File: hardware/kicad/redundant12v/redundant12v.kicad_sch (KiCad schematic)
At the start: 10 parts, among them U1 ATtiny212-SS, U2 MAX232CPE, X1 CXO_DIP8

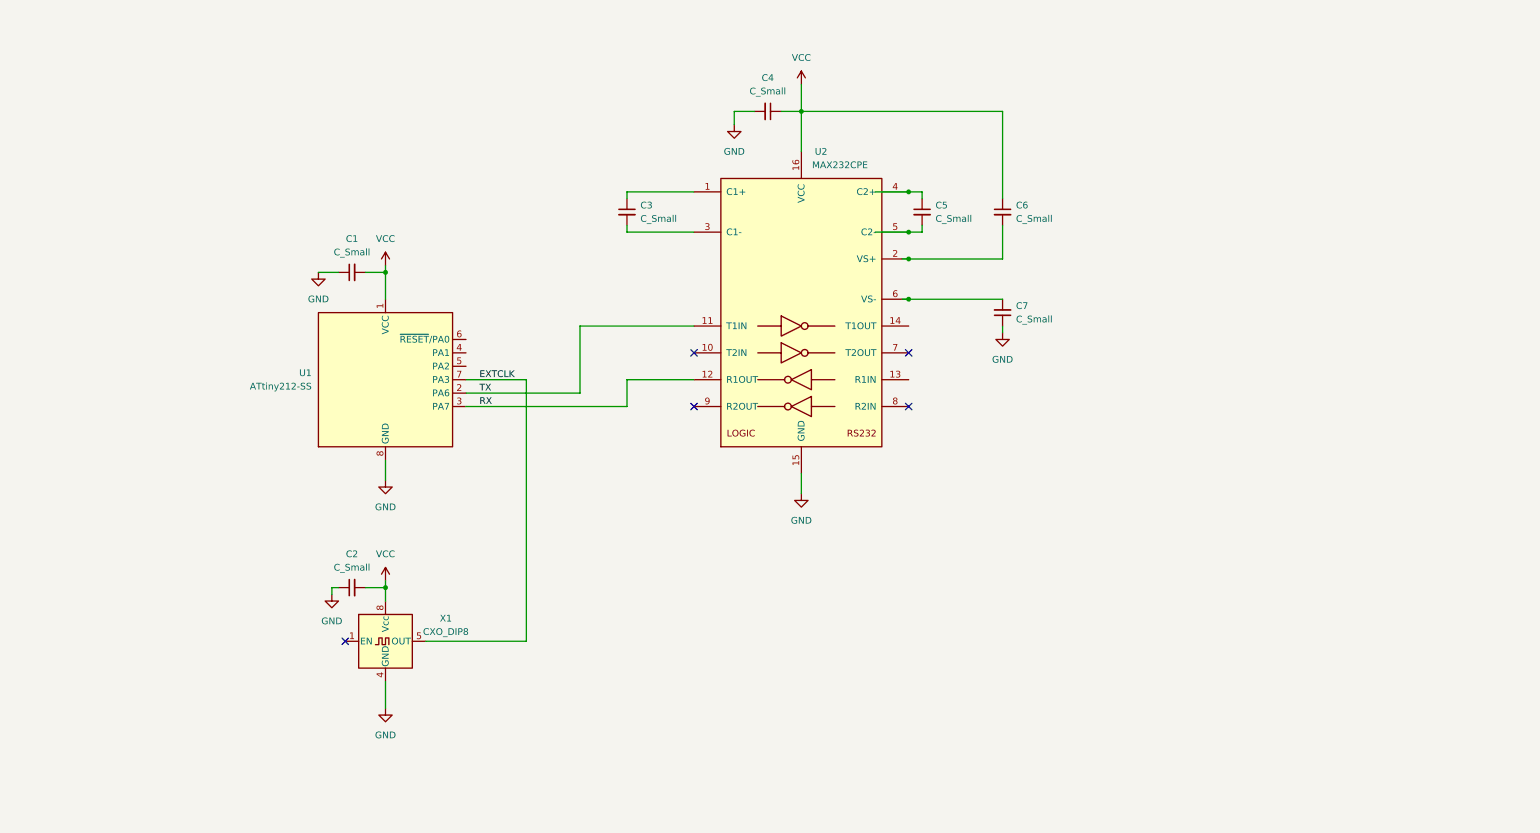
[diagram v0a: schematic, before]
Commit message: Add regulator circuit and LED drivers
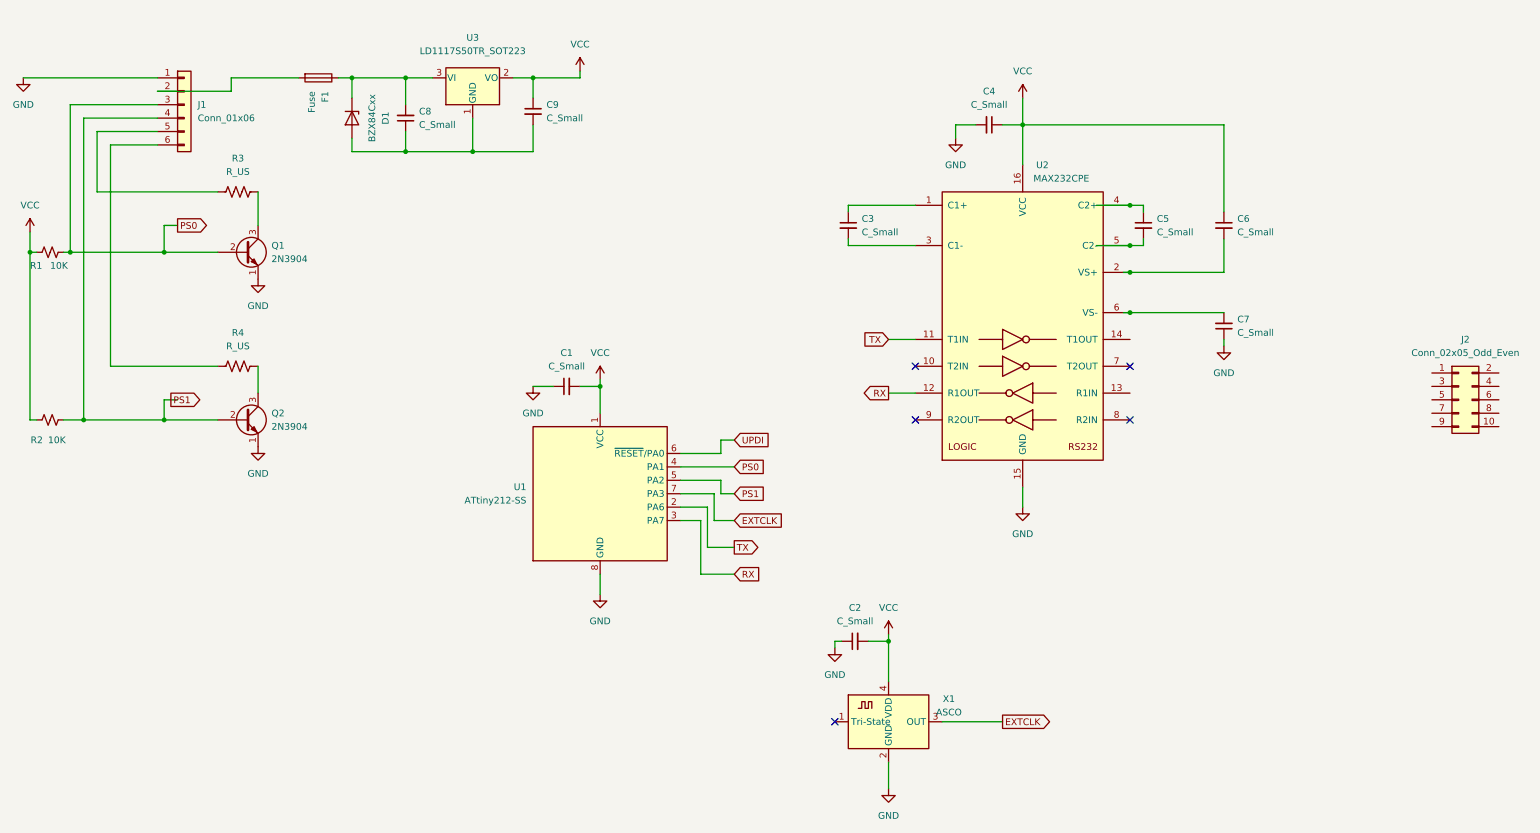
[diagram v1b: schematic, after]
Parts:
- removed X1: CXO_DIP8, Oscillator:Oscillator_DIP-8, symbol Oscillator:CXO_DIP8
- added C8, C9: C_Small, Capacitor_SMD:C_0805_2012Metric_Pad1.18x1.45mm_HandSolder, symbol Device:C_Small
- added D1: BZX84Cxx, Package_TO_SOT_SMD:SOT-23, symbol Diode:BZX84Cxx
- added F1: Fuse, Fuse:Fuse_1206_3216Metric_Pad1.42x1.75mm_HandSolder, symbol Device:Fuse
- added J1: Conn_01x06, Connector_JST:JST_EH_B6B-EH-A_1x06_P2.50mm_Vertical, symbol Connector_Generic:Conn_01x06
- added J2: Conn_02x05_Odd_Even, Connector_IDC:IDC-Header_2x05_P2.54mm_Vertical, symbol Connector_Generic:Conn_02x05_Odd_Even
- added Q1, Q2: 2N3904, Package_TO_SOT_SMD:SOT-23, symbol Transistor_BJT:2N3904
- added R1, R2: 10K, Resistor_SMD:R_0805_2012Metric_Pad1.20x1.40mm_HandSolder, symbol Device:R_Small_US
- added R3, R4: R_US, Resistor_SMD:R_0805_2012Metric_Pad1.20x1.40mm_HandSolder, symbol Device:R_US
- added U3: LD1117S50TR_SOT223, Package_TO_SOT_SMD:SOT-223-3_TabPin2, symbol Regulator_Linear:LD1117S50TR_SOT223
- added X1: ASCO, Oscillator:Oscillator_SMD_Abracon_ASV-4Pin_7.0x5.1mm_HandSoldering, symbol Oscillator:ASCO
- C1, C2, C3, C4, C5, C6, C7: footprint (none) -> Capacitor_SMD:C_0805_2012Metric_Pad1.18x1.45mm_HandSolder
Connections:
- net EXTCLK: now also X1.3 (OUT)
- net GND: now also J1.1 (Pin_1), Q1.1 (E), Q2.1 (E), X1.2 (GND)
- net VCC: now also C9.1, R1.2, R2.2, U3.2 (VO), X1.4 (VDD)
- net PS0: now reaches U1.4 (PA1)
- net PS0: now also J1.3 (Pin_3), Q1.2 (B), R1.1
- net PS1: now reaches U1.5 (PA2)
- net PS1: now also J1.4 (Pin_4), Q2.2 (B), R2.1
- net UPDI: now reaches U1.6 (~{RESET}/PA0)
- new net: J1.6 (Pin_6), R4.1
- new net: Q2.3 (C), R4.2
- new net: C8.2, D1.3 (K), F1.1, U3.3 (VI)
- new net: F1.2, J1.2 (Pin_2)
- new net: C8.1, C9.2, D1.1 (A), U3.1 (GND)
- new net: J1.5 (Pin_5), R3.1
- new net: Q1.3 (C), R3.2
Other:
- moved on the sheet: C1, C2, C3, C4, C5, C6, C7, U1, U2

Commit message: Reorganize schematic, fix LED polarity
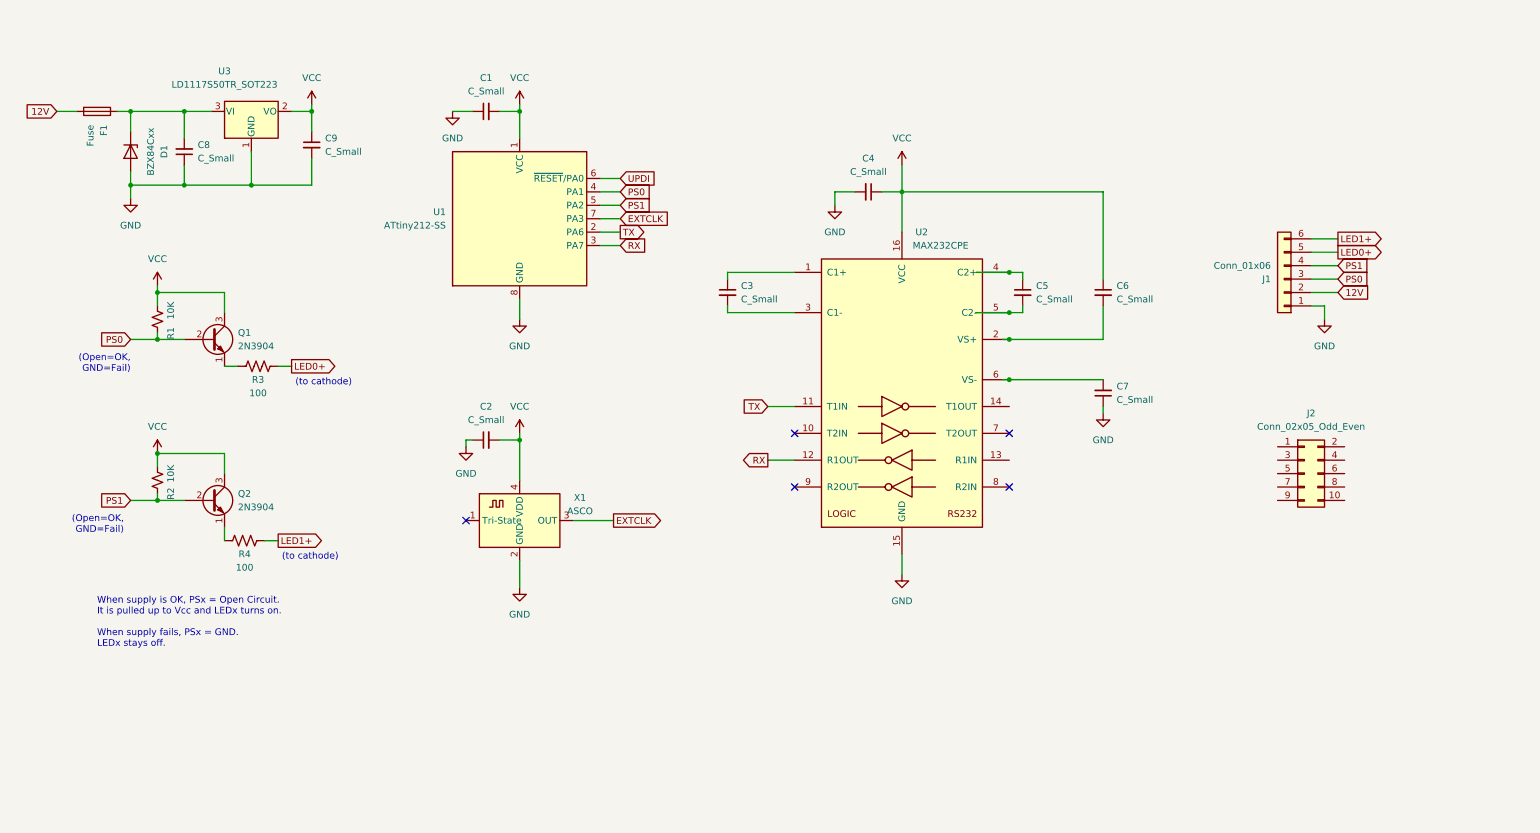
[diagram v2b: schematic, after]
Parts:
- R3, R4: value R_US -> 100
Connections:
- net GND: now also C8.1, C9.2, D1.1 (A), U3.1 (GND); no longer Q1.1 (E), Q2.1 (E)
- net PS0: now also R1.2; no longer R1.1
- net PS1: now also R2.2; no longer R2.1
- net VCC: now also Q1.3 (C), Q2.3 (C), R1.1, R2.1; no longer R1.2, R2.2
- net at R4.1: now also Q2.1 (E); no longer J1.6 (Pin_6)
- net LED1+: now reaches R4.2
- net LED1+: now also J1.6 (Pin_6); no longer Q2.3 (C)
- net 12V: now reaches F1.2, J1.2 (Pin_2)
- net at R3.1: now also Q1.1 (E); no longer J1.5 (Pin_5)
- net LED0+: now reaches R3.2
- net LED0+: now also J1.5 (Pin_5); no longer Q1.3 (C)
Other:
- note added: "(Open=OK, GND=Fail)"
- note added: "(to cathode)"
- note added: "When supply is OK, PSx = Open Circuit. It is pulled up to Vcc and LEDx turns on. When supply fails, PSx = GND. LEDx stays off."
- moved on the sheet: C1, C2, C3, C4, C5, C6, C7, C8, C9, D1, F1, J1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

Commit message: Add serial port connections
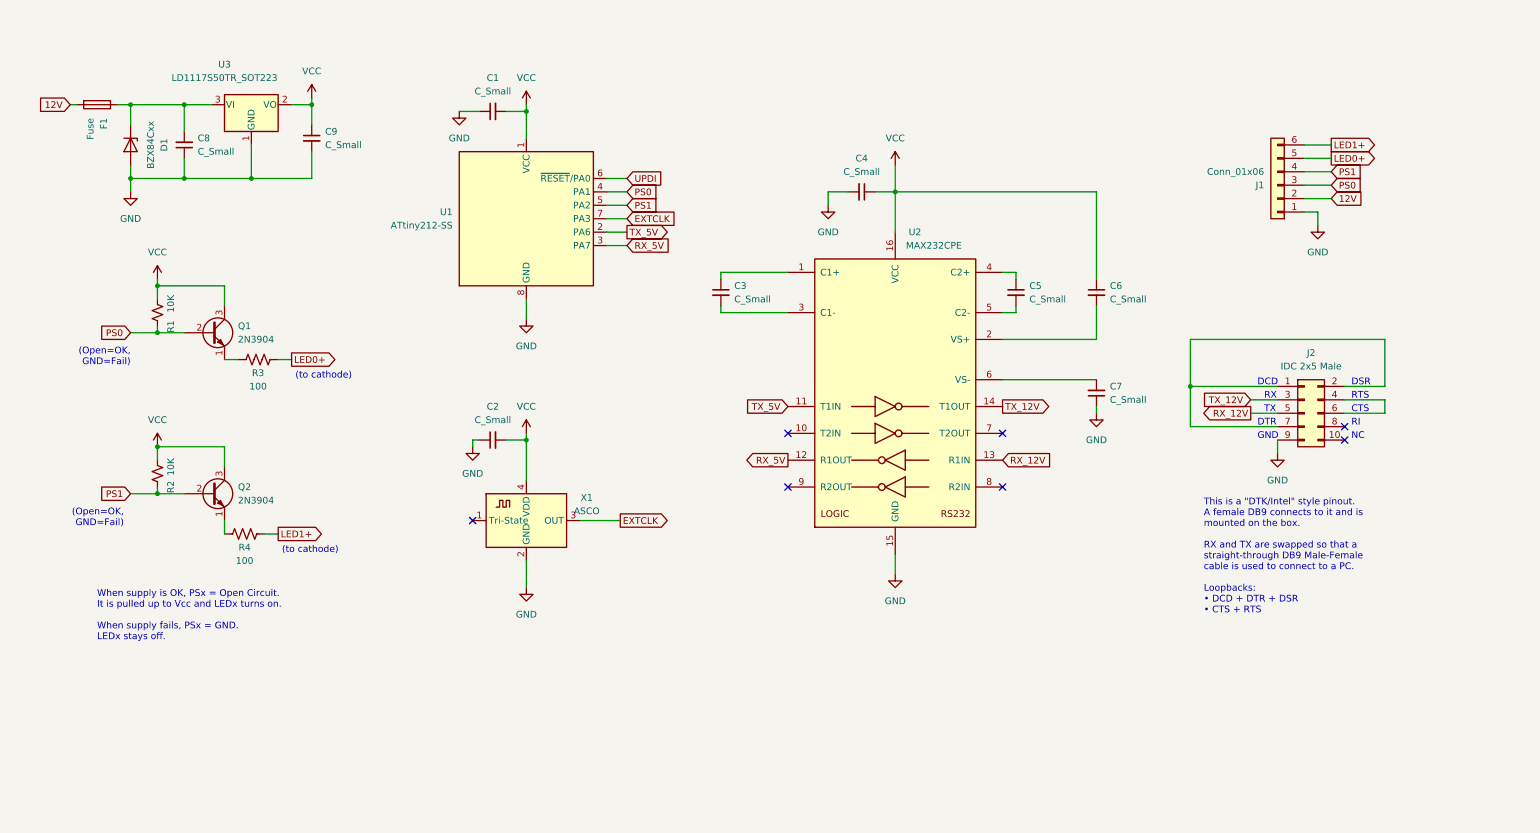
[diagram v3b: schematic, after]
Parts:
- J2: value Conn_02x05_Odd_Even -> IDC 2x5 Male
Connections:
- net GND: now also J2.9 (Pin_9)
- net RX_12V: now reaches U2.13 (R1IN)
- net RX_12V: now also J2.5 (Pin_5)
- net TX_12V: now reaches U2.14 (T1OUT)
- net TX_12V: now also J2.3 (Pin_3)
- net at J2.1 (Pin_1): now also J2.2 (Pin_2), J2.7 (Pin_7)
- net at J2.4 (Pin_4): now also J2.6 (Pin_6)
- net RX renamed RX_5V
- net TX renamed TX_5V
- no-connect marks 5 -> 7
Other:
- note added: "CTS"
- note added: "DCD"
- note added: "DSR"
- note added: "DTR"
- note added: "GND"
- note added: "NC"
- note added: "RI"
- note added: "RTS"
- note added: "RX"
- note added: "TX"
- note added: "This is a "DTK/Intel" style pinout. A female DB9 connects to it and is mounted on the box. RX and TX are swapped so that a straight-through DB9 Male-Female cable is used to connect to a PC. Loopbacks: • DCD + DTR + DSR • CTS + RTS"
- moved on the sheet: C1, C2, C3, C4, C5, C6, C7, C8, C9, D1, F1, J1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

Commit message: PCB is mostly routed
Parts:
- R3, R4: value 100 -> 150
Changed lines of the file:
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@@
     (in_bom yes) (on_board yes)
     (property "Reference" "R4" (id 0) (at 60.96 128.27 90))
-    (property "Value" "100" (id 1) (at 60.96 130.81 90))
+    (property "Value" "150" (id 1) (at 60.96 130.81 90))
     (property "Footprint" "Resistor_SMD:R_0805_2012Metric_Pad1.20x1.40mm_HandSolder" (id 2) (at 61.214 124.714 90)
       (effects (font (size 1.27 1.27)) hide)
@@
     (in_bom yes) (on_board yes)
     (property "Reference" "R3" (id 0) (at 63.5 95.25 90))
-    (property "Value" "100" (id 1) (at 63.5 97.79 90))
+    (property "Value" "150" (id 1) (at 63.5 97.79 90))
     (property "Footprint" "Resistor_SMD:R_0805_2012Metric_Pad1.20x1.40mm_HandSolder" (id 2) (at 63.754 91.694 90)
       (effects (font (size 1.27 1.27)) hide)
@@
     )
     (path "/de0a58e5-7f3d-4ccf-ac8a-4cd50321ae36"
-      (reference "R3") (unit 1) (value "100") (footprint "Resistor_SMD:R_0805_2012Metric_Pad1.20x1.40mm_HandSolder")
+      (reference "R3") (unit 1) (value "150") (footprint "Resistor_SMD:R_0805_2012Metric_Pad1.20x1.40mm_HandSolder")
     )
     (path "/536d55a4-3759-4f62-a47d-eabc58b4f4c3"
-      (reference "R4") (unit 1) (value "100") (footprint "Resistor_SMD:R_0805_2012Metric_Pad1.20x1.40mm_HandSolder")
+      (reference "R4") (unit 1) (value "150") (footprint "Resistor_SMD:R_0805_2012Metric_Pad1.20x1.40mm_HandSolder")
     )
     (path "/18e8ff8f-d1a5-4881-b417-bc839120dcd6"

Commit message: PCB rev 1 finished
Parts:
- added TP1: VTG_5V, TestPoint:TestPoint_Pad_D2.5mm, symbol Connector:TestPoint
- added TP2: UPDI, TestPoint:TestPoint_Pad_D2.5mm, symbol Connector:TestPoint
- added TP3: GND, TestPoint:TestPoint_Pad_D2.5mm, symbol Connector:TestPoint
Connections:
- net GND: now also TP3.1
- net UPDI: now also TP2.1
- net VCC: now also TP1.1
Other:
- moved on the sheet: J1, J2

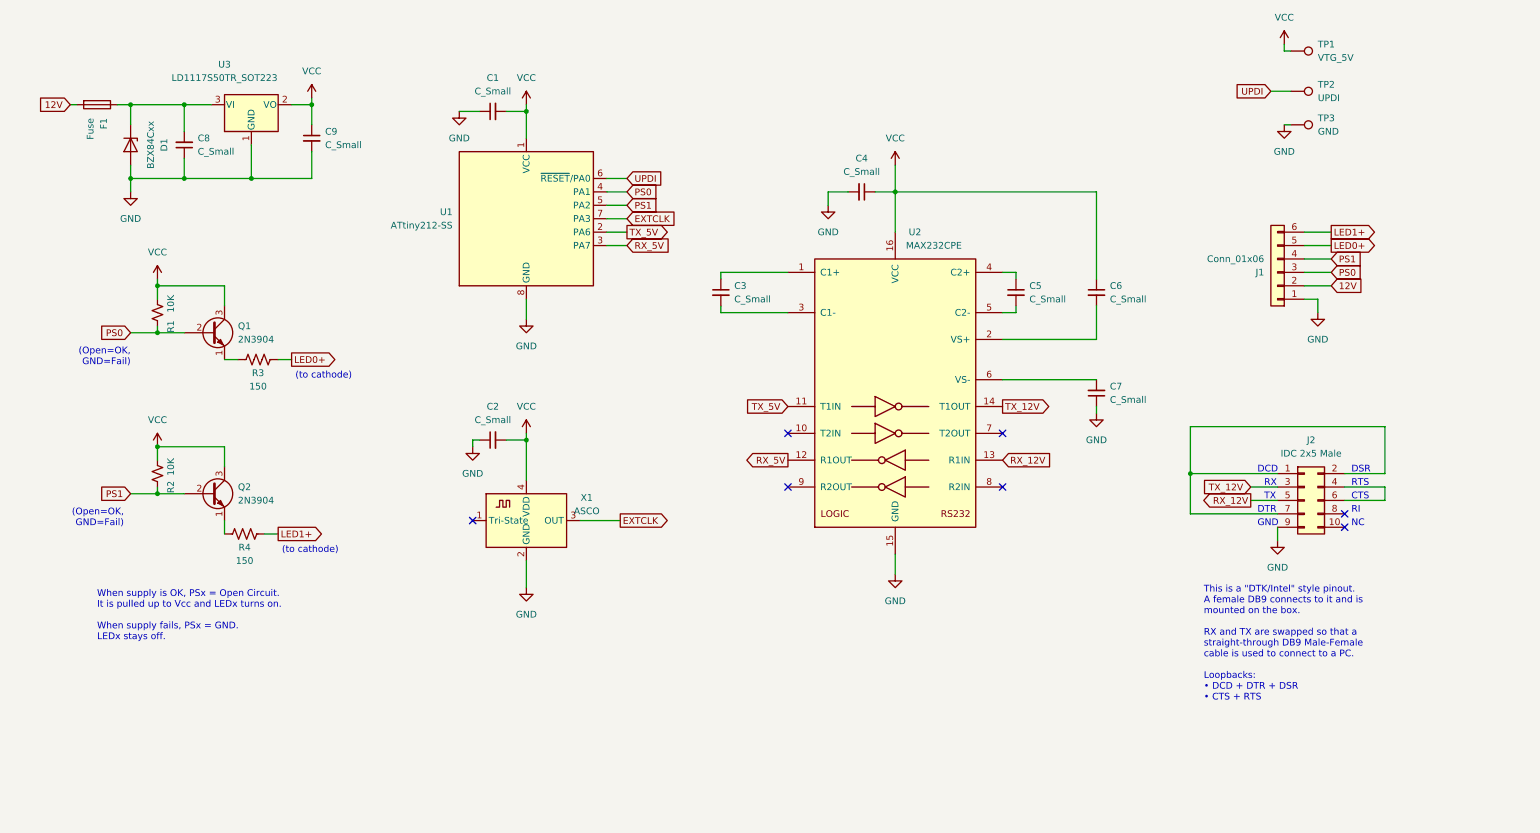
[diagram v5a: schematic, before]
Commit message: Add values to components on schematic
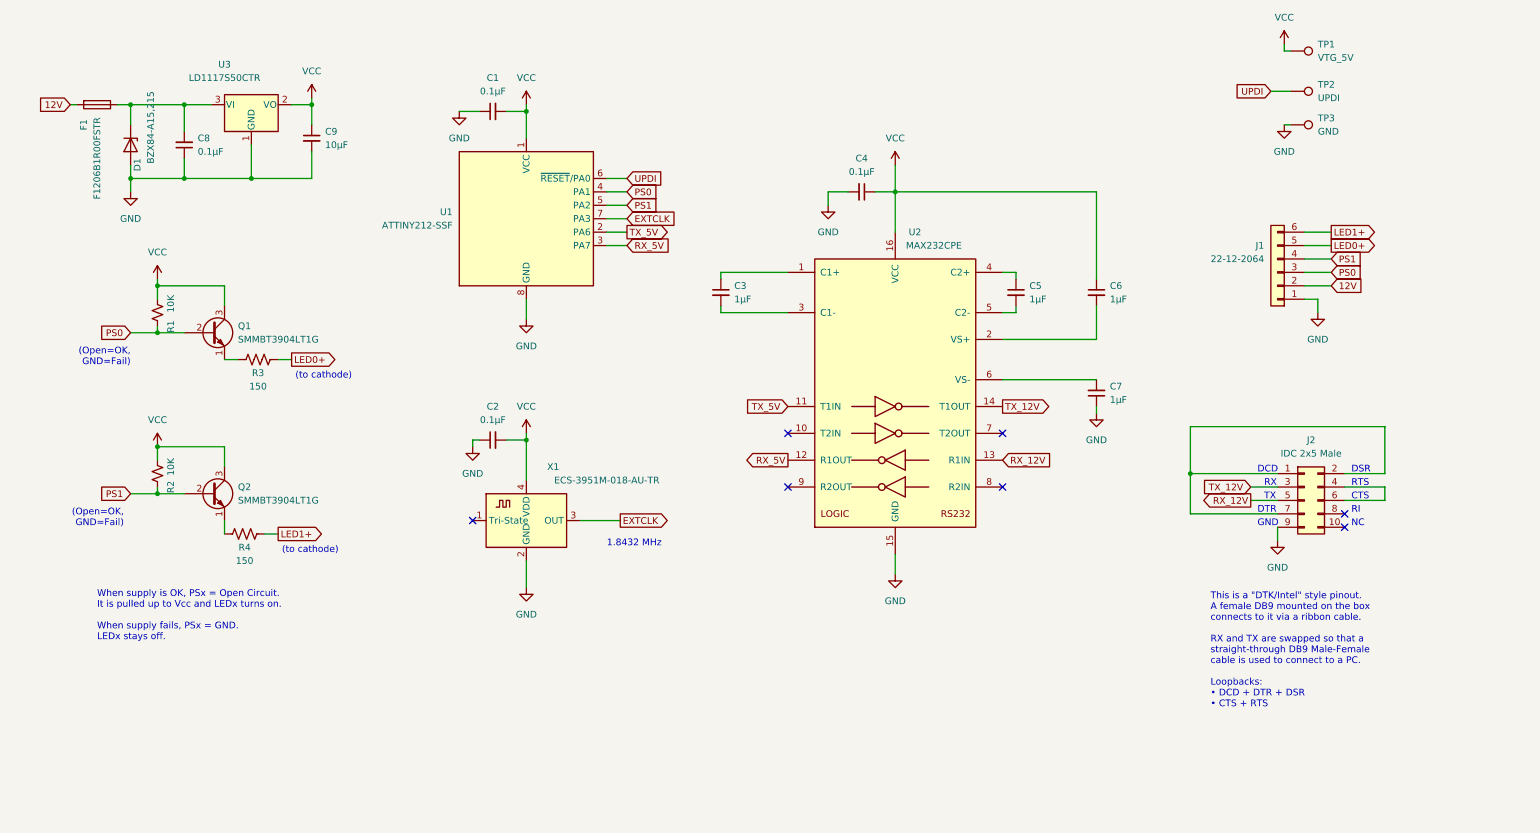
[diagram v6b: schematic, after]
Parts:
- C1, C2, C4, C8: value C_Small -> 0.1μF
- C3, C5, C6, C7: value C_Small -> 1μF
- C9: value C_Small -> 10μF
- D1: value BZX84Cxx -> BZX84-A15,215
- F1: value Fuse -> F1206B1R00FSTR
- J1: value Conn_01x06 -> 22-12-2064
- Q1, Q2: value 2N3904 -> SMMBT3904LT1G
- U1: value ATtiny212-SS -> ATTINY212-SSF
- U3: value LD1117S50TR_SOT223 -> LD1117S50CTR
- X1: value ASCO -> ECS-3951M-018-AU-TR
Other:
- note added: "1.8432 MHz"
- note added: "This is a "DTK/Intel" style pinout. A female DB9 mounted on the box connects to it via a ribbon cable. RX and TX are swapped so that a straight-through DB9 Male-Female cable is used to connect to a PC. Loopbacks: • DCD + DTR + DSR • CTS + RTS"
- note removed: "This is a "DTK/Intel" style pinout. A female DB9 connects to it and is mounted on the box. RX and TX are swapped so that a straight-through DB9 Male-Female cable is used to connect to a PC. Loopbacks: • DCD + DTR + DSR • CTS + RTS"
